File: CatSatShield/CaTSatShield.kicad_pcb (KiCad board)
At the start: 4 copper layers, 67.6 x 25 mm, 17 parts, among them J1 , J2 , J3 BME280, J4 CCS811

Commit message: Routeo
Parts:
- moved J4 44.9 mm to (133.1, 100.1), turned to 90 degrees
- moved J3 37.1 mm to (162.0, 101.6), turned to 90 degrees
- moved G*** 31.1 mm to (172.5, 100.0)
- moved G*** 21.0 mm to (124.5, 100.5)
- moved MODULE1 17.4 mm to (145.5, 100.2)
- moved G*** 9.07 mm to (171.0, 101.5)
- moved @HOLE0 3.77 mm to (116.5, 111.5)
- moved @HOLE1 3.77 mm to (116.5, 91.0)
- moved U$5 3.77 mm to (116.5, 111.5)
- moved U$6 3.77 mm to (116.5, 91.0)
- moved @HOLE2 3.77 mm to (173.5, 91.0)
- moved @HOLE3 3.77 mm to (173.5, 111.5)
- moved U$7 3.77 mm to (173.5, 91.0)
- moved U$8 3.77 mm to (173.5, 111.5)
- moved J1 3.77 mm to (152.7, 112.1)
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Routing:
- net VCC: track 0.00 -> 53.0 mm
- net /SCL: track 0.00 -> 45.5 mm
- net /SDA: track 0.00 -> 42.0 mm
- net /10-INTCCS: track 0.00 -> 30.9 mm
- net GND: track 0.00 -> 30.3 mm
- net +3V3: track 0.00 -> 25.4 mm
- net /RESET: track 0.00 -> 17.4 mm
- net /TX: track 0.00 -> 16.1 mm
- net /RX: track 0.00 -> 5.69 mm
- added copper zone on B.Cu, net GND
- added copper zone on F.Cu, net GND
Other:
- outline, holes or cut-outs redrawn
- net class Default: clearance 0.127 -> 0.2; trace_width 0.25 -> 0.3; via_dia 0.8 -> 1
- net class SOURCE added: clearance 0.2, trace_width 0.5, via_dia 1.2, via_drill 0.6
- rule trace_clearance: 0.127 -> 0.2

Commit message: Best logos
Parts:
- removed the G*** at (172.5, 100.0)
- added G***: LOGO, Aesthetics:catsat_cu, B.Cu at (172.0, 99.6)
- moved G*** 24.1 mm to (148.6, 99.1)
- moved G*** 0.71 mm to (171.7, 101.6)
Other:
- board text added: "*Made on Earth by Humans*"
- board text added: "“To Infinity and Beyond”"
- board text removed: "“to infinity and beyond”"

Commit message: Update logos
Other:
- board text added: "*Designed in Mexico*"
- board text removed: "*Made on Earth by Humans*"
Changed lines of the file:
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@@
   )
   (layers
-    (0 Top signal)
+    (0 Top signal hide)
     (1 LFSignals signal hide)
     (2 POWER signal hide)
-    (31 Bottom signal)
+    (31 Bottom signal hide)
     (32 B.Adhes user)
     (33 F.Adhes user)
@@
       (effects (font (size 1 1) (thickness 0.25)) (justify left bottom mirror))
     )
-    (fp_text value BME280 (at 5.08 2.52 90) (layer B.SilkS)
+    (fp_text value BME280 (at 2.774 -1.706 90) (layer B.SilkS)
       (effects (font (size 1 1) (thickness 0.25)) (justify left bottom mirror))
     )
@@
       (xy -8.236377 -5.397363) (xy -8.174627 -5.397401)) (layer B.Mask) (width 0.01))
   )
-  (gr_text "*Made on Earth \nby Humans*" (at 123.952 100.584 90) (layer F.SilkS)
+  (gr_text "*Designed \nin \nMexico*" (at 123.952 100.584 90) (layer F.SilkS)
     (effects (font (size 1.5 1.5) (thickness 0.3)))
   )

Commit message: Remove extra layers
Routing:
- removed copper zone on LFSignals, net (none)
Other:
- copper layers 4 -> 2
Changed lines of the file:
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@@
   )
   (layers
-    (0 Top signal hide)
-    (1 LFSignals signal hide)
-    (2 POWER signal hide)
-    (31 Bottom signal hide)
+    (0 Top signal)
+    (31 Bottom signal)
     (32 B.Adhes user)
     (33 F.Adhes user)
@@
     (38 B.Mask user)
     (39 F.Mask user)
-    (40 Dwgs.User user hide)
+    (40 Dwgs.User user)
     (41 Cmts.User user)
     (42 Eco1.User user)
     (43 Eco2.User user)
     (44 Edge.Cuts user)
-    (45 Margin user hide)
+    (45 Margin user)
     (46 B.CrtYd user)
     (47 F.CrtYd user)
     (48 B.Fab user)
-    (49 F.Fab user hide)
+    (49 F.Fab user)
   )
   (setup
@@
   (segment (start 158.18 96.25) (end 159.08 95.35) (width 0.3) (layer Top) (net 33))
   (segment (start 133.14 96.25) (end 158.18 96.25) (width 0.3) (layer Top) (net 33))
-  (zone (net 0) (net_name "") (layer LFSignals) (hatch edge 0.508)
-    (priority 6)
-    (connect_pads (clearance 0))
-    (min_thickness 0.254)
-    (fill yes (arc_segments 32) (thermal_gap 0.304) (thermal_bridge_width 0.304))
-    (polygon
-      (pts
-        (xy 114.237479 109.2636) (xy 114.237479 93.2136) (xy 118.687479 93.2136) (xy 118.687479 88.7636) (xy 135.037479 88.7636)
-        (xy 135.037479 92.7636) (xy 142.337479 92.7636) (xy 142.337479 88.7636) (xy 145.537479 88.7636) (xy 145.537479 92.3636)
-        (xy 167.762479 92.3636) (xy 167.762479 108.7636) (xy 167.762479 110.1636) (xy 135.037479 110.1636) (xy 135.037479 113.7636)
-        (xy 118.737479 113.7636) (xy 118.737479 109.2636)
-      )
-    )
-  )
   (zone (net 2) (net_name GND) (layer Top) (hatch edge 0.508)
     (connect_pads (clearance 0.508))

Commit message: Update version 0.2-beta
Fix Tx and RX, add logo OSHW
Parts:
- added REF***: OSHW-Logo_5.7x6mm_SilkScreen, Symbols:OSHW-Logo_5.7x6mm_SilkScreen, F.Cu at (124.0, 102.6)
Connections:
- MODULE1 pad 1: /RX -> /TX
- MODULE1 pad 2: /TX -> /RX
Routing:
- net /TX: track 16.1 -> 7.99 mm
- net /RX: track 5.69 -> 13.3 mm, vias 0 -> 1
- net /RESET: track 17.4 -> 15.4 mm
- net /10-INTCCS: track 30.9 -> 32.2 mm
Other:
- board text removed: "*Designed in Mexico*"

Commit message: change connector header x socker J4
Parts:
- J4: footprint Pines:62000811121 -> Connector_PinSocket_2.54mm:PinSocket_1x08_P2.54mm_Vertical; moved to F.Cu
- moved J4 10.1 mm to (130.9, 109.9), turned to 180 degrees
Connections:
- J3 pad 1: VCC -> +3V3
- J4 pad 1: VCC -> +3V3
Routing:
- net VCC: track 52.8 -> 0.00 mm
- net +3V3: track 25.4 -> 0.00 mm
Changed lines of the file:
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@@
-(kicad_pcb (version 20171130) (host pcbnew "(5.0.0-3-g5ebb6b6)")
+(kicad_pcb (version 20171130) (host pcbnew "(5.0.0)")
   (general
     (thickness 1.6)
     (drawings 53)
-    (tracks 66)
+    (tracks 52)
     (zones 0)
     (modules 18)
@@
     (35 F.Paste user)
     (36 B.SilkS user)
-    (37 F.SilkS user)
+    (37 F.SilkS user hide)
     (38 B.Mask user)
     (39 F.Mask user)
-    (40 Dwgs.User user)
+    (40 Dwgs.User user hide)
     (41 Cmts.User user)
     (42 Eco1.User user)
@@
     (add_net VCC)
   )
-  (module Pines:62000811121 (layer Bottom)
-    (at 133.14 100.06 90)
-    (descr "WR-PHD 2.00mm Pin Header, 8 Pins")
-    (fp_text reference J4 (at -7.94 2.36 90) (layer B.SilkS)
-      (effects (font (size 1 1) (thickness 0.25)) (justify left bottom mirror))
-    )
-    (fp_text value CCS811 (at 10.06 -1.64 90) (layer B.SilkS)
-      (effects (font (size 1 1) (thickness 0.25)) (justify left bottom mirror))
-    )
-    (fp_line (start -10 -1) (end 10 -1) (layer B.SilkS) (width 0.127))
-    (fp_line (start 10 -1) (end 10 1) (layer B.SilkS) (width 0.127))
-    (fp_line (start 10 1) (end -10 1) (layer B.SilkS) (width 0.127))
-    (fp_line (start -10 1) (end -10 -1) (layer B.SilkS) (width 0.127))
-    (fp_text user 1 (at -9 -0.75 90) (layer Cmts.User)
-      (effects (font (size 1.2065 1.2065) (thickness 0.1016)) (justify left bottom))
-    )
-    (pad 1 thru_hole rect (at -8.89 0 90) (size 1.308 1.308) (drill 0.8) (layers *.Cu *.Mask)
-      (net 22 VCC))
-    (pad 2 thru_hole circle (at -6.35 0 90) (size 1.308 1.308) (drill 0.8) (layers *.Cu *.Mask)
-      (net 2 GND))
-    (pad 3 thru_hole circle (at -3.81 0 90) (size 1.308 1.308) (drill 0.8) (layers *.Cu *.Mask)
-      (net 31 /SCL))
-    (pad 4 thru_hole circle (at -1.27 0 90) (size 1.308 1.308) (drill 0.8) (layers *.Cu *.Mask)
-      (net 32 /SDA))
-    (pad 5 thru_hole circle (at 1.27 0 90) (size 1.308 1.308) (drill 0.8) (layers *.Cu *.Mask)
-      (net 34 /WAK-A6))
-    (pad 6 thru_hole circle (at 3.81 0 90) (size 1.308 1.308) (drill 0.8) (layers *.Cu *.Mask)
-      (net 33 /10-INTCCS))
-    (pad 7 thru_hole circle (at 6.35 0 90) (size 1.308 1.308) (drill 0.8) (layers *.Cu *.Mask)
-      (net 23 /RESET))
-    (pad 8 thru_hole circle (at 8.89 0 90) (size 1.308 1.308) (drill 0.8) (layers *.Cu *.Mask)
-      (net 1 "Net-(J4-Pad8)"))
-  )
   (module Rf:QUECTEL_L80-M39 (layer Bottom)
     (at 145.5 100.22)
@@
     )
     (pad 1 thru_hole rect (at -3.81 0 90) (size 1.65 1.65) (drill 1.1) (layers *.Cu *.Mask)
-      (net 22 VCC))
+      (net 3 +3V3))
     (pad 2 thru_hole circle (at -1.27 0 90) (size 1.65 1.65) (drill 1.1) (layers *.Cu *.Mask)
       (net 2 GND))
@@
       (xy 0.376964 -2.709982)) (layer F.SilkS) (width 0.01))
   )
+  (module Connector_PinSocket_2.54mm:PinSocket_1x08_P2.54mm_Vertical (layer Top)
+    (at 130.9 109.9 180)
+    (descr "Through hole straight socket strip, 1x08, 2.54mm pitch, single row (from Kicad 4.0.7), script generated")
+    (tags "Through hole socket strip THT 1x08 2.54mm single row")
+    (fp_text reference J4 (at 0 -2.77 180) (layer F.SilkS)
+      (effects (font (size 1 1) (thickness 0.15)))
+    )
+    (fp_text value CCS811 (at 0 20.55 180) (layer F.Fab)
+      (effects (font (size 1 1) (thickness 0.15)))
+    )
+    (fp_line (start -1.27 -1.27) (end 0.635 -1.27) (layer F.Fab) (width 0.1))
+    (fp_line (start 0.635 -1.27) (end 1.27 -0.635) (layer F.Fab) (width 0.1))
+    (fp_line (start 1.27 -0.635) (end 1.27 19.05) (layer F.Fab) (width 0.1))
+    (fp_line (start 1.27 19.05) (end -1.27 19.05) (layer F.Fab) (width 0.1))
+    (fp_line (start -1.27 19.05) (end -1.27 -1.27) (layer F.Fab) (width 0.1))
+    (fp_line (start -1.33 1.27) (end 1.33 1.27) (layer F.SilkS) (width 0.12))
+    (fp_line (start -1.33 1.27) (end -1.33 19.11) (layer F.SilkS) (width 0.12))
+    (fp_line (start -1.33 19.11) (end 1.33 19.11) (layer F.SilkS) (width 0.12))
+    (fp_line (start 1.33 1.27) (end 1.33 19.11) (layer F.SilkS) (width 0.12))
+    (fp_line (start 1.33 -1.33) (end 1.33 0) (layer F.SilkS) (width 0.12))
+    (fp_line (start 0 -1.33) (end 1.33 -1.33) (layer F.SilkS) (width 0.12))
+    (fp_line (start -1.8 -1.8) (end 1.75 -1.8) (layer F.CrtYd) (width 0.05))
+    (fp_line (start 1.75 -1.8) (end 1.75 19.55) (layer F.CrtYd) (width 0.05))
+    (fp_line (start 1.75 19.55) (end -1.8 19.55) (layer F.CrtYd) (width 0.05))
+    (fp_line (start -1.8 19.55) (end -1.8 -1.8) (layer F.CrtYd) (width 0.05))
+    (fp_text user %R (at 0 8.89 270) (layer F.Fab)
+      (effects (font (size 1 1) (thickness 0.15)))
+    )
+    (pad 1 thru_hole rect (at 0 0 180) (size 1.7 1.7) (drill 1) (layers *.Cu *.Mask)
+      (net 3 +3V3))
+    (pad 2 thru_hole oval (at 0 2.54 180) (size 1.7 1.7) (drill 1) (layers *.Cu *.Mask)
+      (net 2 GND))
+    (pad 3 thru_hole oval (at 0 5.08 180) (size 1.7 1.7) (drill 1) (layers *.Cu *.Mask)
+      (net 31 /SCL))
+    (pad 4 thru_hole oval (at 0 7.62 180) (size 1.7 1.7) (drill 1) (layers *.Cu *.Mask)
+      (net 32 /SDA))
+    (pad 5 thru_hole oval (at 0 10.16 180) (size 1.7 1.7) (drill 1) (layers *.Cu *.Mask)
+      (net 34 /WAK-A6))
+    (pad 6 thru_hole oval (at 0 12.7 180) (size 1.7 1.7) (drill 1) (layers *.Cu *.Mask)
+      (net 33 /10-INTCCS))
+    (pad 7 thru_hole oval (at 0 15.24 180) (size 1.7 1.7) (drill 1) (layers *.Cu *.Mask)
+      (net 23 /RESET))
+    (pad 8 thru_hole oval (at 0 17.78 180) (size 1.7 1.7) (drill 1) (layers *.Cu *.Mask)
+      (net 1 "Net-(J4-Pad8)"))
+    (model ${KISYS3DMOD}/Connector_PinSocket_2.54mm.3dshapes/PinSocket_1x08_P2.54mm_Vertical.wrl
+      (at (xyz 0 0 0))
+      (scale (xyz 1 1 1))
+      (rotate (xyz 0 0 0))
+    )
+  )
   (dimension 20.391081 (width 0.3) (layer Margin)
     (gr_text "20.391 mm" (at 171.665993 106.887428 -0.5900778959) (layer Margin)
@@
   (segment (start 156.63 102.85) (end 161.98 102.85) (width 0.5) (layer Top) (net 2))
   (segment (start 153.07 106.41) (end 156.63 102.85) (width 0.5) (layer Top) (net 2))
-  (segment (start 141.282 100.852) (end 141.282 90.748) (width 0.5) (layer Bottom) (net 3))
-  (segment (start 142.77 102.34) (end 141.282 100.852) (width 0.5) (layer Bottom) (net 3))
-  (segment (start 142.77 102.34) (end 153.4 102.34) (width 0.5) (layer Bottom) (net 3))
-  (segment (start 153.4 104.88) (end 153.4 102.34) (width 0.5) (layer Bottom) (net 3))
-  (segment (start 161.98 105.39) (end 158.53 105.39) (width 0.5) (layer Top) (net 22))
-  (segment (start 154.97 108.95) (end 133.14 108.95) (width 0.5) (layer Top) (net 22))
-  (segment (start 158.53 105.39) (end 154.97 108.95) (width 0.5) (layer Top) (net 22))
-  (segment (start 138.742 91.85) (end 138.742 90.748) (width 0.5) (layer Bottom) (net 22))
-  (segment (start 138.092 92.5) (end 138.742 91.85) (width 0.5) (layer Bottom) (net 22))
-  (segment (start 135 93.4) (end 135.9 92.5) (width 0.5) (layer Bottom) (net 22))
-  (segment (start 135.9 92.5) (end 138.092 92.5) (width 0.5) (layer Bottom) (net 22))
-  (segment (start 135 108.244) (end 135 93.4) (width 0.5) (layer Bottom) (net 22))
-  (segment (start 134.294 108.95) (end 135 108.244) (width 0.5) (layer Bottom) (net 22))
-  (segment (start 133.14 108.95) (end 134.294 108.95) (width 0.5) (layer Bottom) (net 22))
   (segment (start 146.362 92.35) (end 146.362 90.748) (width 0.3) (layer Top) (net 23))
   (segment (start 134.064895 93.71) (end 134.080895 93.726) (width 0.3) (layer Top) (net 23))

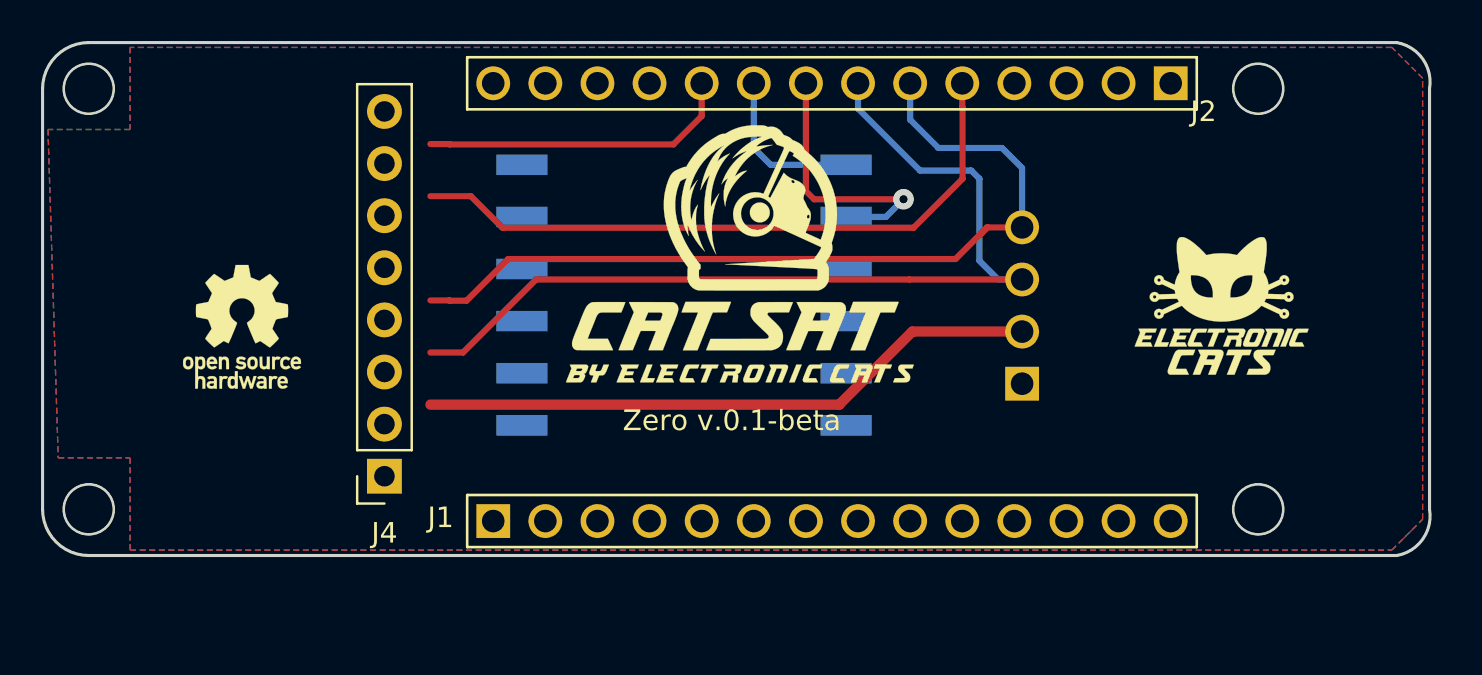
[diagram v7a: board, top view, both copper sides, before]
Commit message: routeo change voltage
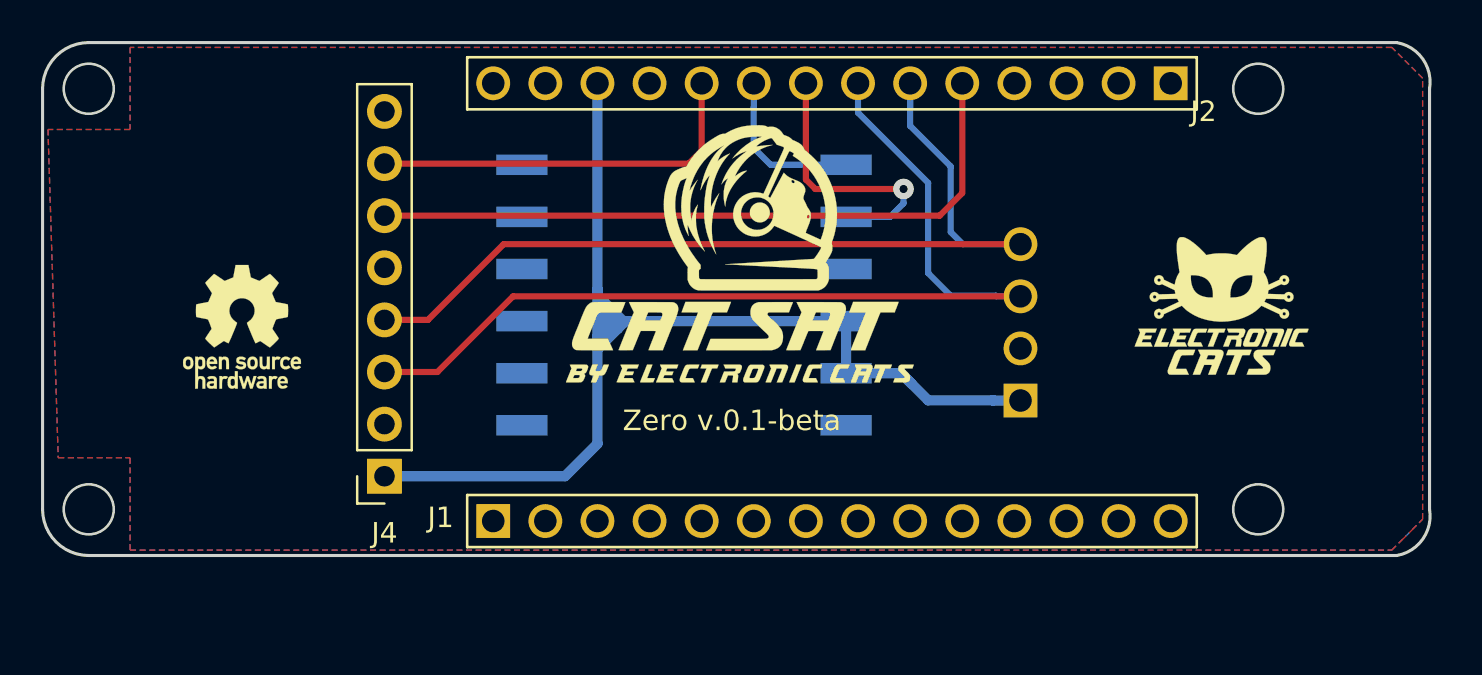
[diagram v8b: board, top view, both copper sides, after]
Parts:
- moved J3 0.82 mm to (161.9, 102.4)
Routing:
- net +3V3: track 0.00 -> 59.7 mm
- net GND: track 30.3 -> 0.00 mm
- net /RESET: track 15.4 -> 19.0 mm
- net /SDA: track 41.9 -> 45.4 mm
- net /SCL: track 45.3 -> 48.2 mm
- net /10-INTCCS: track 32.2 -> 34.0 mm
